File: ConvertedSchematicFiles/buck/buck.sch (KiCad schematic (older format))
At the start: 19 parts, among them IC1 IC1, M1 IRF150

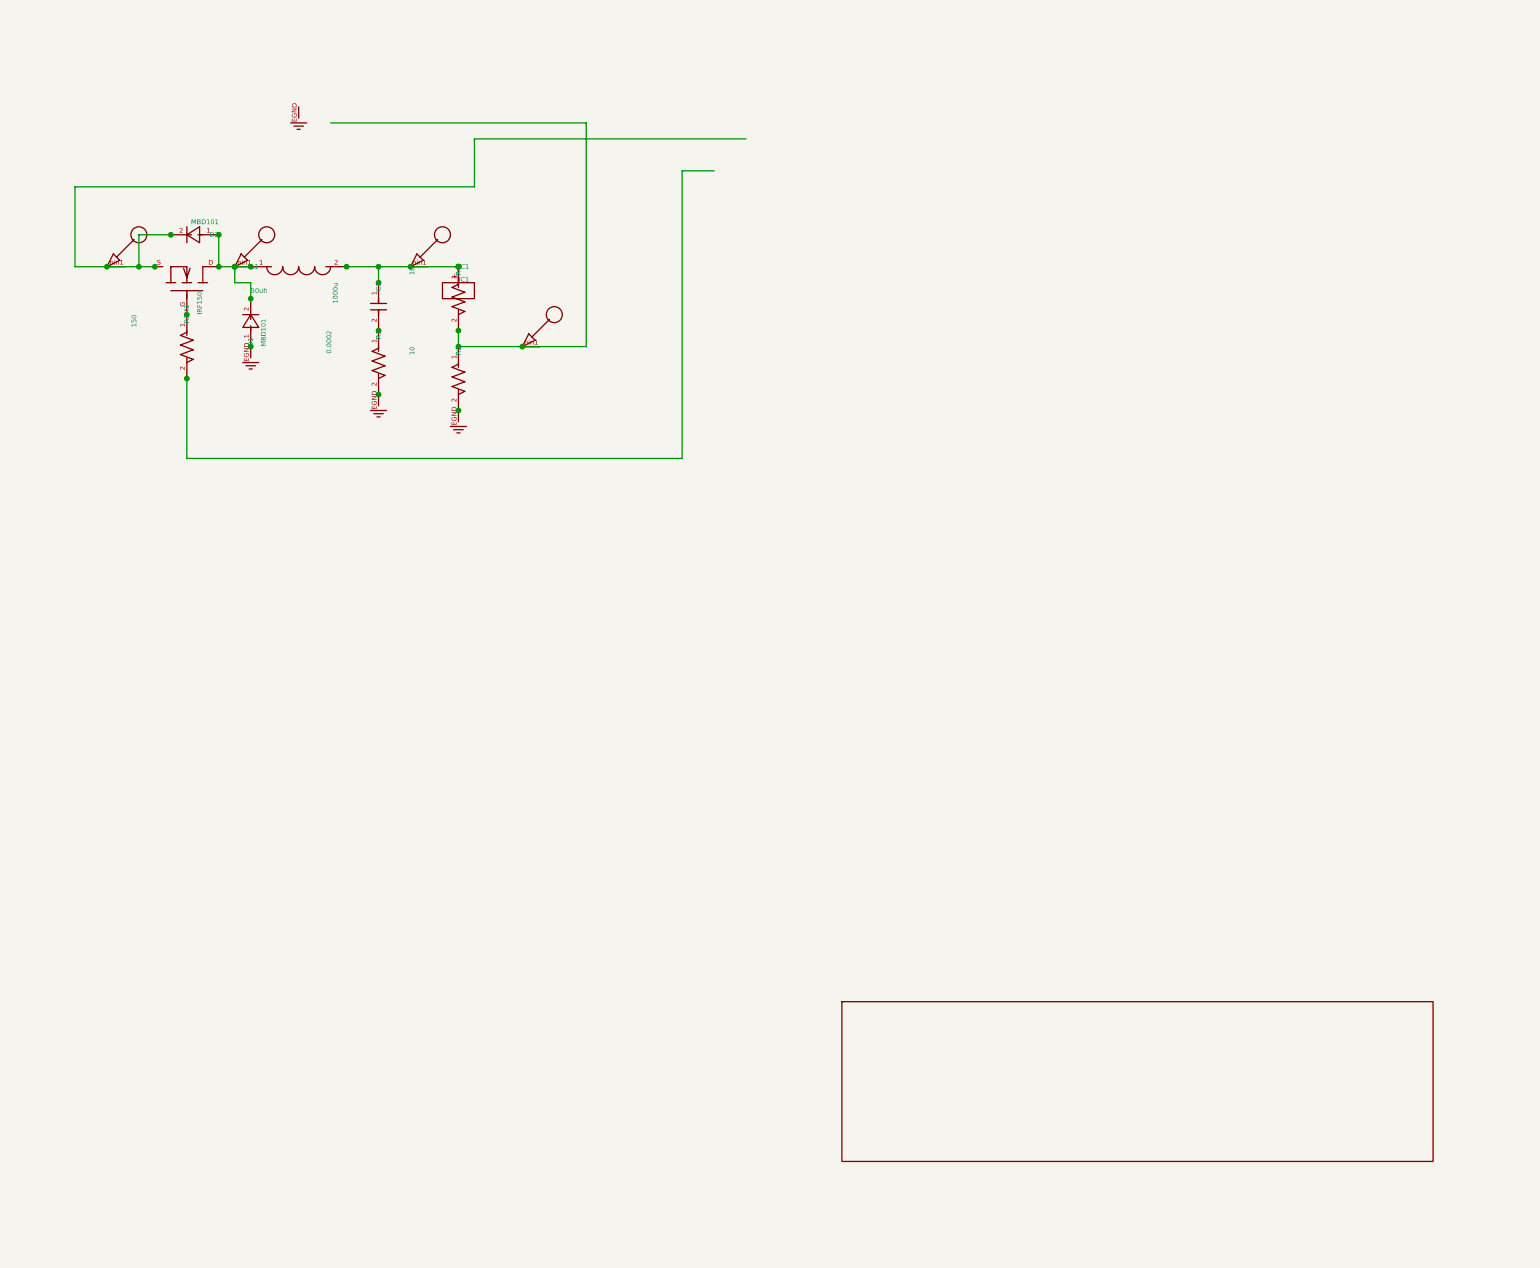
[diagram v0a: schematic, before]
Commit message: Excluded some components. These no longer appear after conversion. When calling shell commands, filenames are in "quotes"
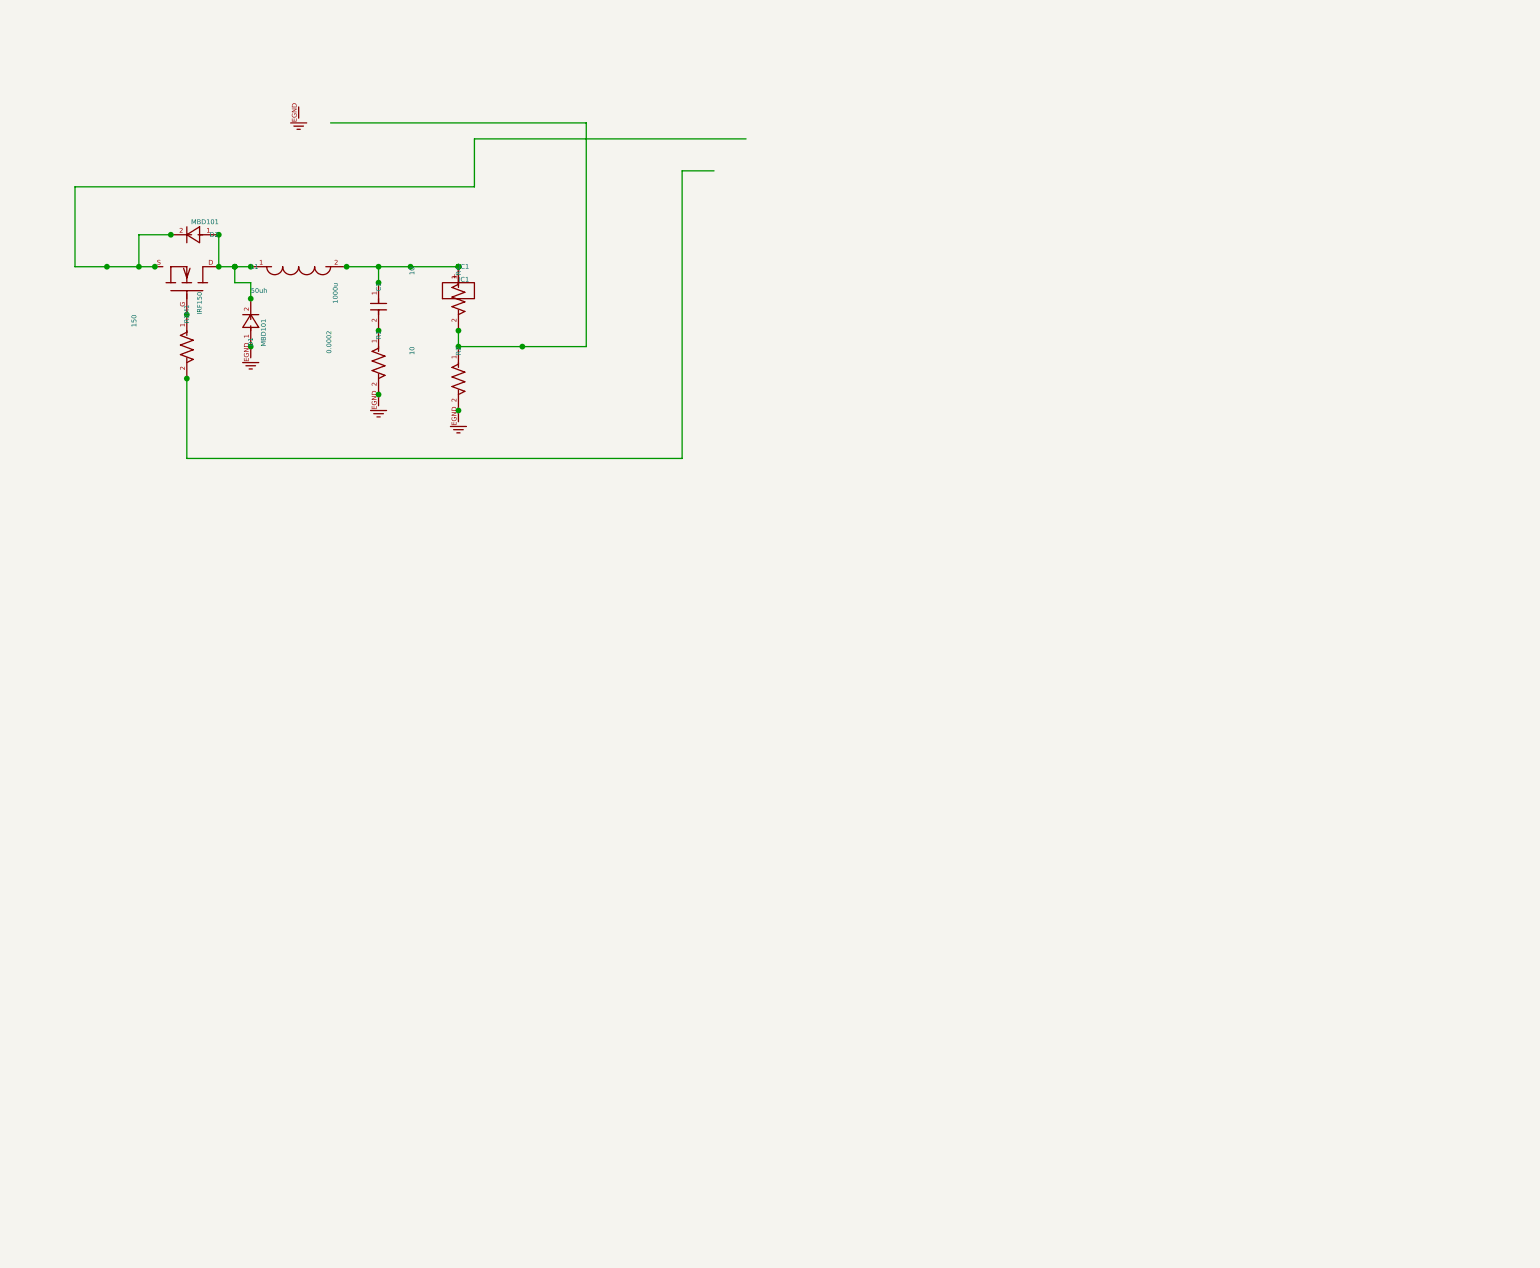
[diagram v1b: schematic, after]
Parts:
- removed nodeMarker (x2): nodeMarker, symbol NODEMARKER_PSPICE
- removed titleblk: titleblk, symbol TITLEBLK_PSPICE
- removed vdiffMarker (x2): vdiffMarker, symbol VDIFFMARKER_PSPICE
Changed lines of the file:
@@
 	-1    0    0    -1
-$EndComp
-$Comp
-L TITLEBLK_PSPICE titleblk
-U 1 1 74897763
-P 9700 7200
-F 0 "titleblk" H 19400 14400 30  0001 L CNN
-F 1 "titleblk" H 19400 14480 30  0001 L CNN
-	1    9700 7200
-	1    0    0    1
-$EndComp
-$Comp
-L VDIFFMARKER_PSPICE vdiffMarker
-U 1 1 87513926
-P 2200 1600
-F 0 "vdiffMarker" H 4400 3200 30  0001 L CNN
-F 1 "vdiffMarker" H 4400 3280 30  0001 L CNN
-	1    2200 1600
-	1    0    0    1
-$EndComp
-$Comp
-L NODEMARKER_PSPICE nodeMarker
-U 1 1 25180540
-P 4000 2100
-F 0 "nodeMarker" H 8000 4200 30  0001 L CNN
-F 1 "nodeMarker" H 8000 4280 30  0001 L CNN
-	1    4000 2100
-	1    0    0    1
-$EndComp
-$Comp
-L NODEMARKER_PSPICE nodeMarker
-U 1 1 20383426
-P 3300 1600
-F 0 "nodeMarker" H 6600 3200 30  0001 L CNN
-F 1 "nodeMarker" H 6600 3280 30  0001 L CNN
-	1    3300 1600
-	1    0    0    1
-$EndComp
-$Comp
-L VDIFFMARKER_PSPICE vdiffMarker
-U 1 1 44089172
-P 1400 1600
-F 0 "vdiffMarker" H 2800 3200 30  0001 L CNN
-F 1 "vdiffMarker" H 2800 3280 30  0001 L CNN
-	1    1400 1600
-	1    0    0    1
 $EndComp
 Wire Wire Line

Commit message: Ports issue fixed. Now annotation for ports is #PWR? function added "itos"
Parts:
- removed EGND (x4): EGND, symbol EGND_PSPICE
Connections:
- net labels added: EGND
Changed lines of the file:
@@
 $EndDescr
 $Comp
-L EGND_PSPICE EGND
+L EGND_PSPICE #PWR1
 U 1 1 14289383
 P 2600 600
-F 0 "EGND" H 5200 1200 30  0001 L CNN
+F 0 "#PWR1" H 5200 1200 30  0001 L CNN
 F 1 "EGND" H 5200 1280 30  0001 L CNN
 	1    2600 600
@@
 $EndComp
 $Comp
-L EGND_PSPICE EGND
+L EGND_PSPICE #PWR2
 U 1 1 46930886
 P 3600 2500
-F 0 "EGND" H 7200 5000 30  0001 L CNN
+F 0 "#PWR2" H 7200 5000 30  0001 L CNN
 F 1 "EGND" H 7200 5080 30  0001 L CNN
 	1    3600 2500
@@
 $EndComp
 $Comp
-L EGND_PSPICE EGND
+L EGND_PSPICE #PWR3
 U 1 1 71692777
 P 3100 2400
-F 0 "EGND" H 6200 4800 30  0001 L CNN
+F 0 "#PWR3" H 6200 4800 30  0001 L CNN
 F 1 "EGND" H 6200 4880 30  0001 L CNN
 	1    3100 2400
@@
 $EndComp
 $Comp
-L EGND_PSPICE EGND
+L EGND_PSPICE #PWR4
 U 1 1 14636915
 P 2300 2100
-F 0 "EGND" H 4600 4200 30  0001 L CNN
+F 0 "#PWR4" H 4600 4200 30  0001 L CNN
 F 1 "EGND" H 4600 4280 30  0001 L CNN
 	1    2300 2100

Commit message: Added LICENSE.txt
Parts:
- renumbered M1 to Q?
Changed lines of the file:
@@
 $EndDescr
 $Comp
-L EGND_PSPICE #PWR1
+L GND #PWR1
 U 1 1 14289383
 P 2600 600
@@
 $EndComp
 $Comp
-L EGND_PSPICE #PWR2
+L GND #PWR2
 U 1 1 46930886
 P 3600 2500
@@
 $EndComp
 $Comp
-L EGND_PSPICE #PWR3
+L GND #PWR3
 U 1 1 71692777
 P 3100 2400
@@
 $EndComp
 $Comp
-L EGND_PSPICE #PWR4
+L GND #PWR4
 U 1 1 14636915
 P 2300 2100
@@
 $EndComp
 $Comp
-L IRF150_PSPICE M1
+L IRF150_PSPICE Q?
 U 1 1 73368690
 P 1900 1900
-F 0 "M1" H 1900 1900 30  0000 L CNN
+F 0 "Q?" H 1900 1900 30  0000 L CNN
 F 1 "IRF150" H 1900 1980 30  0000 L CNN
 	1    1900 1900

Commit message: Orientation fix. Library components are now inverted, with +ve y axis going up. In Schematic files, +ve y axis is downwards. This is how the KiCad libraries are. As a result of the above fixed, the converted GND is now oriented correctly.
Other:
- moved on the sheet: IC1, L1
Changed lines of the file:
@@
 F 1 "EGND" H 5200 1280 30  0001 L CNN
 	1    2600 600
-	1    0    0    1
+	1    0    0    -1
 $EndComp
 $Comp
@@
 F 1 "EGND" H 7200 5080 30  0001 L CNN
 	1    3600 2500
-	1    0    0    1
+	1    0    0    -1
 $EndComp
 $Comp
@@
 F 1 "EGND" H 6200 4880 30  0001 L CNN
 	1    3100 2400
-	1    0    0    1
+	1    0    0    -1
 $EndComp
 $Comp
@@
 F 1 "EGND" H 4600 4280 30  0001 L CNN
 	1    2300 2100
-	1    0    0    1
+	1    0    0    -1
 $EndComp
 $Comp
@@
 F 1 "0.0002" H 3100 2310 30  0000 L CNN
 	1    3100 2000
-	0    -1    1    0
+	0    1    1    0
 $EndComp
 $Comp
@@
 F 1 "MBD101" H 2300 2180 30  0000 L CNN
 	1    2300 2100
-	0    1    -1    0
+	0    -1    -1    0
 $EndComp
 $Comp
@@
 F 1 "10" H 3600 2390 30  0000 L CNN
 	1    3600 2100
-	0    -1    1    0
+	0    1    1    0
 $EndComp
 $Comp
@@
 F 1 "150" H 1900 2230 30  0000 L CNN
 	1    1900 1900
-	0    -1    1    0
+	0    1    1    0
 $EndComp
 $Comp
@@
 F 1 "IC1" H 3600 1680 30  0000 L CNN
 	1    3600 1600
-	1    0    0    1
+	1    0    0    -1
 $EndComp
 $Comp
@@
 F 1 "10" H 3600 1890 30  0000 L CNN
 	1    3600 1600
-	0    -1    1    0
+	0    1    1    0
 $EndComp
 $Comp
@@
 F 1 "50uh" H 2300 1750 30  0000 L CNN
 	1    2300 1600
-	1    0    0    1
+	1    0    0    -1
 $EndComp
 $Comp
@@
 F 1 "1000u" H 3100 1970 30  0000 L CNN
 	1    3100 1700
-	0    -1    1    0
+	0    1    1    0
 $EndComp
 $Comp
@@
 F 1 "IRF150" H 1900 1980 30  0000 L CNN
 	1    1900 1900
-	0    1    -1    0
+	0    -1    -1    0
 $EndComp
 $Comp
@@
 F 1 "MBD101" H 2100 1480 30  0000 L CNN
 	1    2100 1400
-	-1    0    0    -1
+	-1    0    0    1
 $EndComp
 Wire Wire Line

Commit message: Removed the use of exec, wrote basename function, made integration with eSim easier.
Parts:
- added nodeMarker (x2): nodeMarker, symbol nodeMarker_PSPICE
- added titleblk: titleblk, symbol titleblk_PSPICE
- added vdiffMarker (x2): vdiffMarker, symbol vdiffMarker_PSPICE
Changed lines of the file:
@@
-EESchema Schematic File Version 2  date Sunday 20 June 1999 02:41:04 AM IST
+EESchema Schematic File Version 2  date
 LIBS:power
 LIBS:device
@@
 LIBS:contrib
 LIBS:valves
-LIBS:ConvertedSchematicFiles/buck-cache
 EELAYER 25  0
 EELAYER END
@@
 Sheet 1 1
 Title ""
-Date "20 Jun 1999"
+Date ""
 Rev ""
 Comp ""
@@
 	-1    0    0    1
 $EndComp
+$Comp
+L titleblk_PSPICE titleblk
+U 1 1 74897763
+P 9700 7200
+F 0 "titleblk" H 19400 14400 30  0001 L CNN
+F 1 "titleblk" H 19400 14480 30  0001 L CNN
+	1    9700 7200
+	1    0    0    -1
+$EndComp
+$Comp
+L vdiffMarker_PSPICE vdiffMarker
+U 1 1 87513926
+P 2200 1600
+F 0 "vdiffMarker" H 4400 3200 30  0001 L CNN
+F 1 "vdiffMarker" H 4400 3280 30  0001 L CNN
+	1    2200 1600
+	1    0    0    -1
+$EndComp
+$Comp
+L nodeMarker_PSPICE nodeMarker
+U 1 1 25180540
+P 4000 2100
+F 0 "nodeMarker" H 8000 4200 30  0001 L CNN
+F 1 "nodeMarker" H 8000 4280 30  0001 L CNN
+	1    4000 2100
+	1    0    0    -1
+$EndComp
+$Comp
+L nodeMarker_PSPICE nodeMarker
+U 1 1 20383426
+P 3300 1600
+F 0 "nodeMarker" H 6600 3200 30  0001 L CNN
+F 1 "nodeMarker" H 6600 3280 30  0001 L CNN
+	1    3300 1600
+	1    0    0    -1
+$EndComp
+$Comp
+L vdiffMarker_PSPICE vdiffMarker
+U 1 1 44089172
+P 1400 1600
+F 0 "vdiffMarker" H 2800 3200 30  0001 L CNN
+F 1 "vdiffMarker" H 2800 3280 30  0001 L CNN
+	1    1400 1600
+	1    0    0    -1
+$EndComp
 Wire Wire Line
